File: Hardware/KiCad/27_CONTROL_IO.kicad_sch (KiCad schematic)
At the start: 0 parts

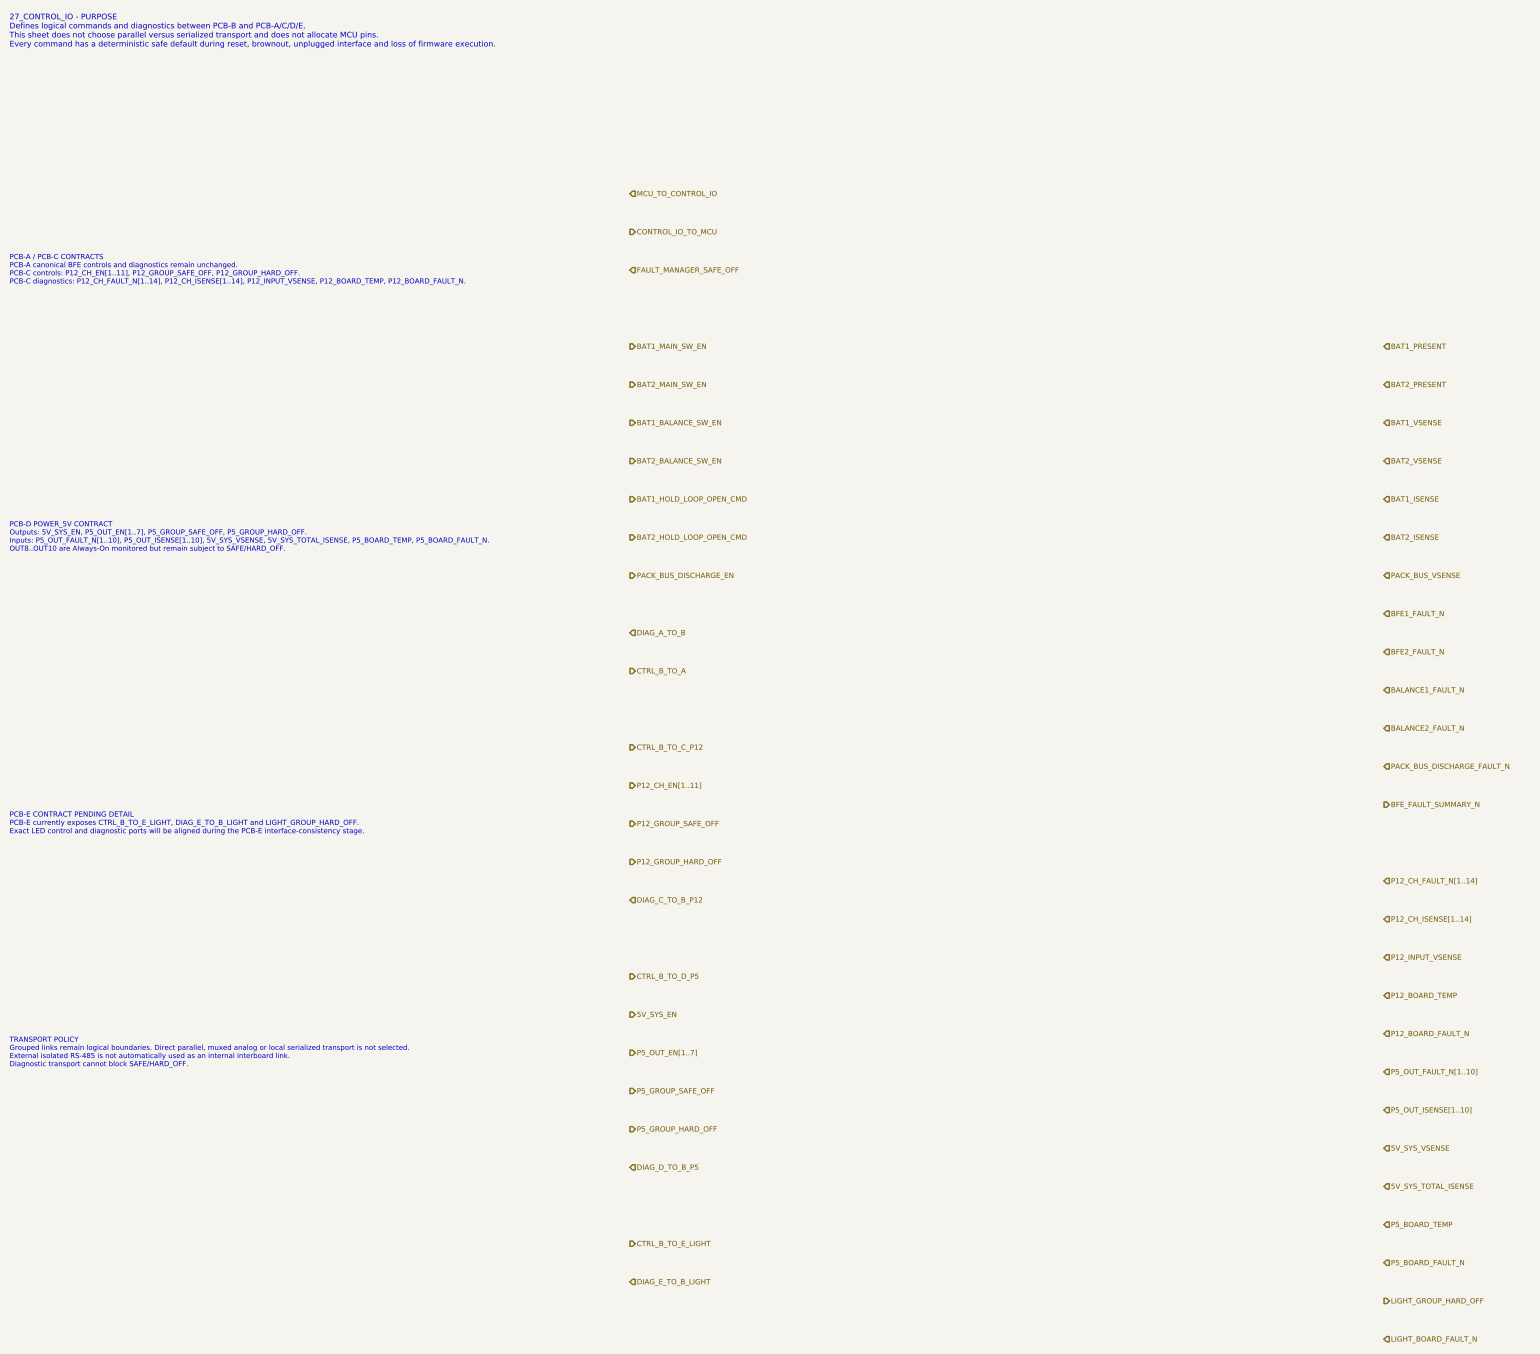
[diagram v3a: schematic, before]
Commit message: hardware: replace parallel channel pins with CAN-FD data-object boundary
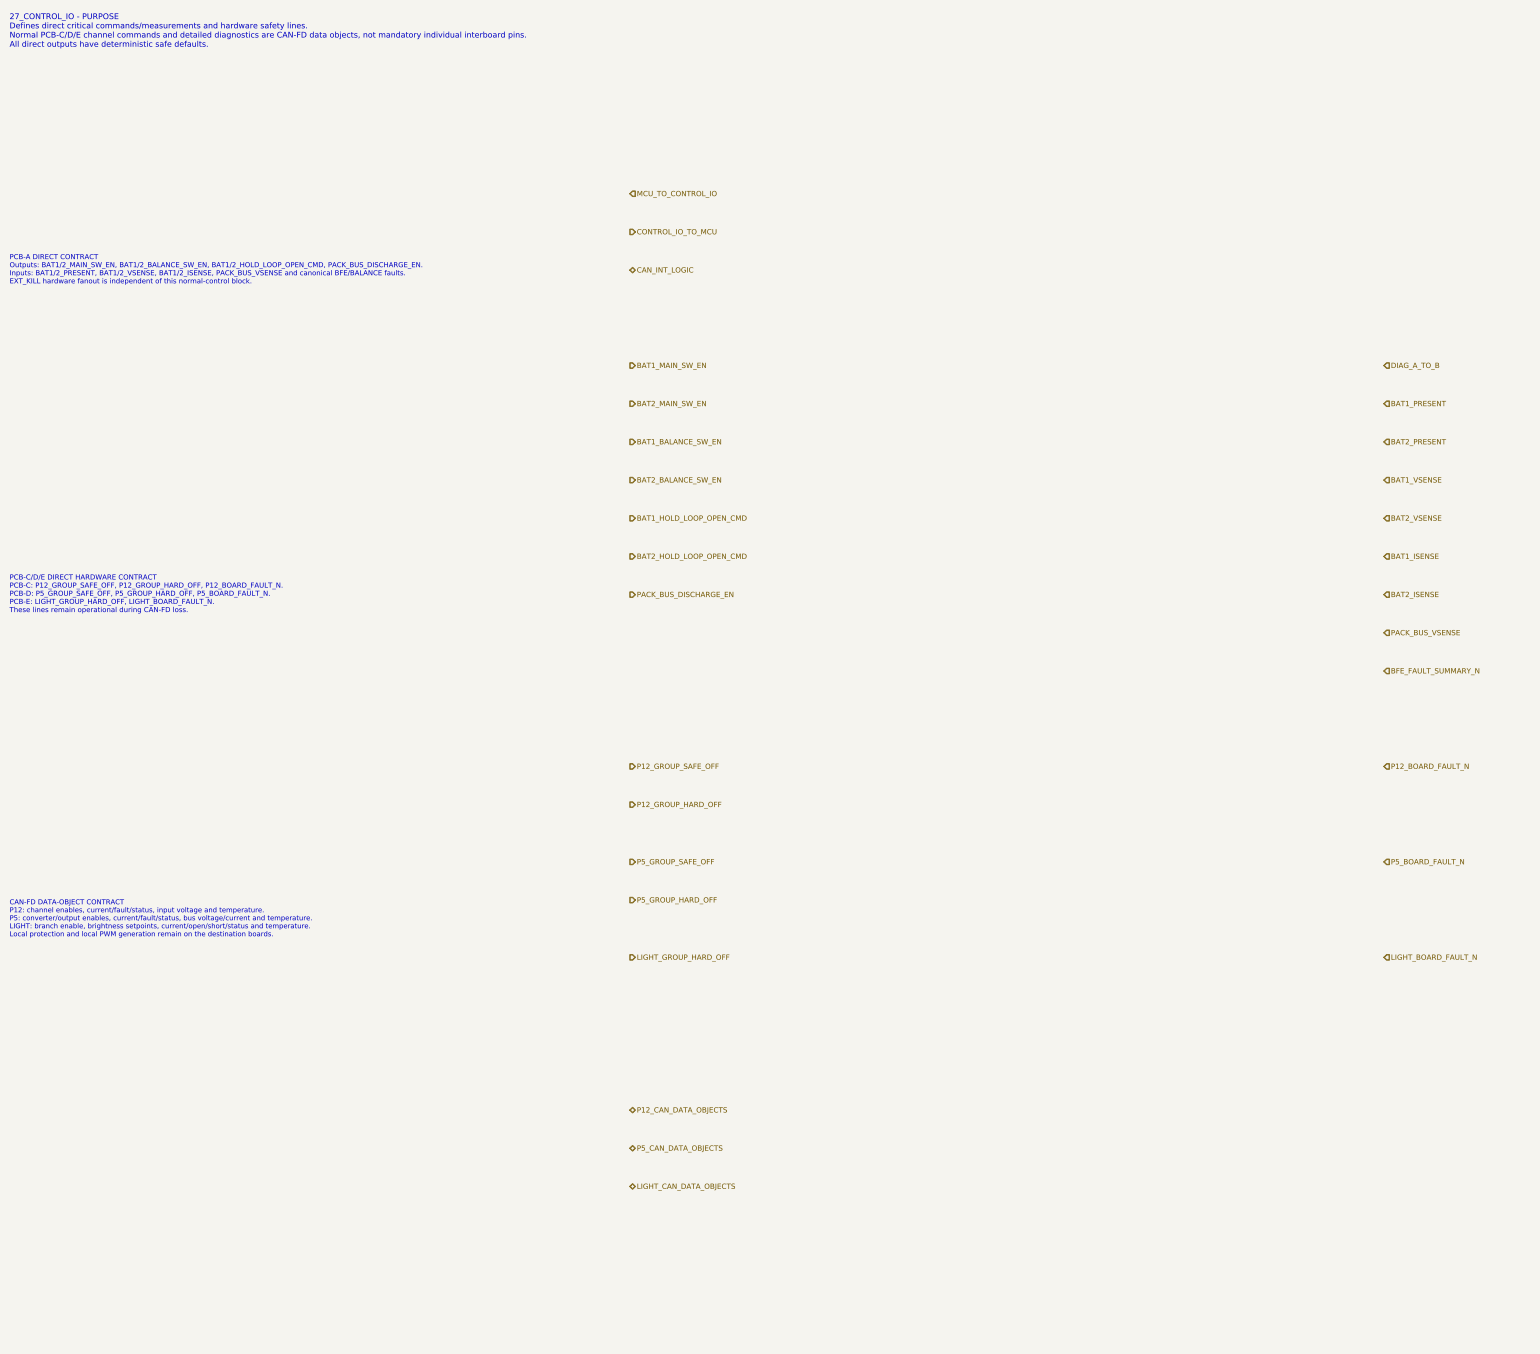
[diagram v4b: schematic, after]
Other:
- note added: "27_CONTROL_IO - PURPOSE Defines direct critical commands/measurements and hardware safety lines. Normal PCB-C/D/E channel commands and detailed diagnostics are CAN-FD data objects, not mandatory individual interboard pins. All direct outputs have deterministic safe defaults."
- note added: "CAN-FD DATA-OBJECT CONTRACT P12: channel enables, current/fault/status, input voltage and temperature. P5: converter/output enables, current/fault/status, bus voltage/current and temperature. LIGHT: branch enable, brightness setpoints, current/open/short/status and temperature. Local protection and local PWM generation remain on the destination boards."
- note added: "PCB-A DIRECT CONTRACT Outputs: BAT1/2_MAIN_SW_EN, BAT1/2_BALANCE_SW_EN, BAT1/2_HOLD_LOOP_OPEN_CMD, PACK_BUS_DISCHARGE_EN. Inputs: BAT1/2_PRESENT, BAT1/2_VSENSE, BAT1/2_ISENSE, PACK_BUS_VSENSE and canonical BFE/BALANCE faults. EXT_KILL hardware fanout is independent of this normal-control block."
- note added: "PCB-C/D/E DIRECT HARDWARE CONTRACT PCB-C: P12_GROUP_SAFE_OFF, P12_GROUP_HARD_OFF, P12_BOARD_FAULT_N. PCB-D: P5_GROUP_SAFE_OFF, P5_GROUP_HARD_OFF, P5_BOARD_FAULT_N. PCB-E: LIGHT_GROUP_HARD_OFF, LIGHT_BOARD_FAULT_N. These lines remain operational during CAN-FD loss."
- note removed: "27_CONTROL_IO - PURPOSE Defines logical commands and diagnostics between PCB-B and PCB-A/C/D/E. This sheet does not choose parallel versus serialized transport and does not allocate MCU pins. Every command has a deterministic safe default during reset, brownout, unplugged interface and loss of firmware execution."
- note removed: "PCB-A / PCB-C CONTRACTS PCB-A canonical BFE controls and diagnostics remain unchanged. PCB-C controls: P12_CH_EN[1..11], P12_GROUP_SAFE_OFF, P12_GROUP_HARD_OFF. PCB-C diagnostics: P12_CH_FAULT_N[1..14], P12_CH_ISENSE[1..14], P12_INPUT_VSENSE, P12_BOARD_TEMP, P12_BOARD_FAULT_N."
- note removed: "PCB-D POWER_5V CONTRACT Outputs: 5V_SYS_EN, P5_OUT_EN[1..7], P5_GROUP_SAFE_OFF, P5_GROUP_HARD_OFF. Inputs: P5_OUT_FAULT_N[1..10], P5_OUT_ISENSE[1..10], 5V_SYS_VSENSE, 5V_SYS_TOTAL_ISENSE, P5_BOARD_TEMP, P5_BOARD_FAULT_N. OUT8..OUT10 are Always-On monitored but remain subject to SAFE/HARD_OFF."
- note removed: "PCB-E CONTRACT PENDING DETAIL PCB-E currently exposes CTRL_B_TO_E_LIGHT, DIAG_E_TO_B_LIGHT and LIGHT_GROUP_HARD_OFF. Exact LED control and diagnostic ports will be aligned during the PCB-E interface-consistency stage."
- note removed: "TRANSPORT POLICY Grouped links remain logical boundaries. Direct parallel, muxed analog or local serialized transport is not selected. External isolated RS-485 is not automatically used as an internal interboard link. Diagnostic transport cannot block SAFE/HARD_OFF."
- title: 27_CONTROL_IO - interboard control and diagnostics boundary -> 27_CONTROL_IO - direct safety and CAN-FD data boundary
